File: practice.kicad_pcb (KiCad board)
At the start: 2 copper layers, 100 x 100 mm, 190 parts, among them U1 LTC1742, U10 LTC1742, U2 LTC1742, U3 LTC1742, U4 LTC1742, U5 LTC1742, U6 LTC1742, U7 LTC1742, U8 LTC1742, U9 LTC1742

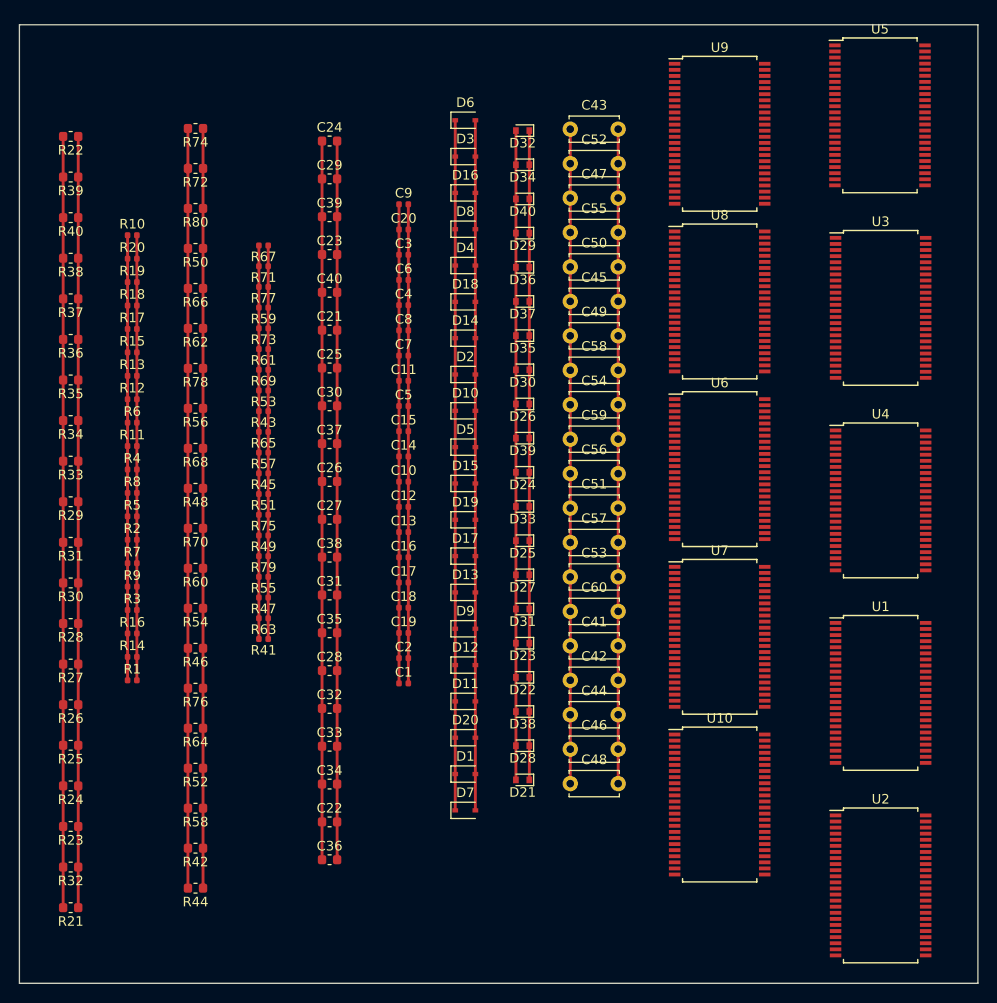
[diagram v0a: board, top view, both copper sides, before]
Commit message: change some part cuz i find them useless
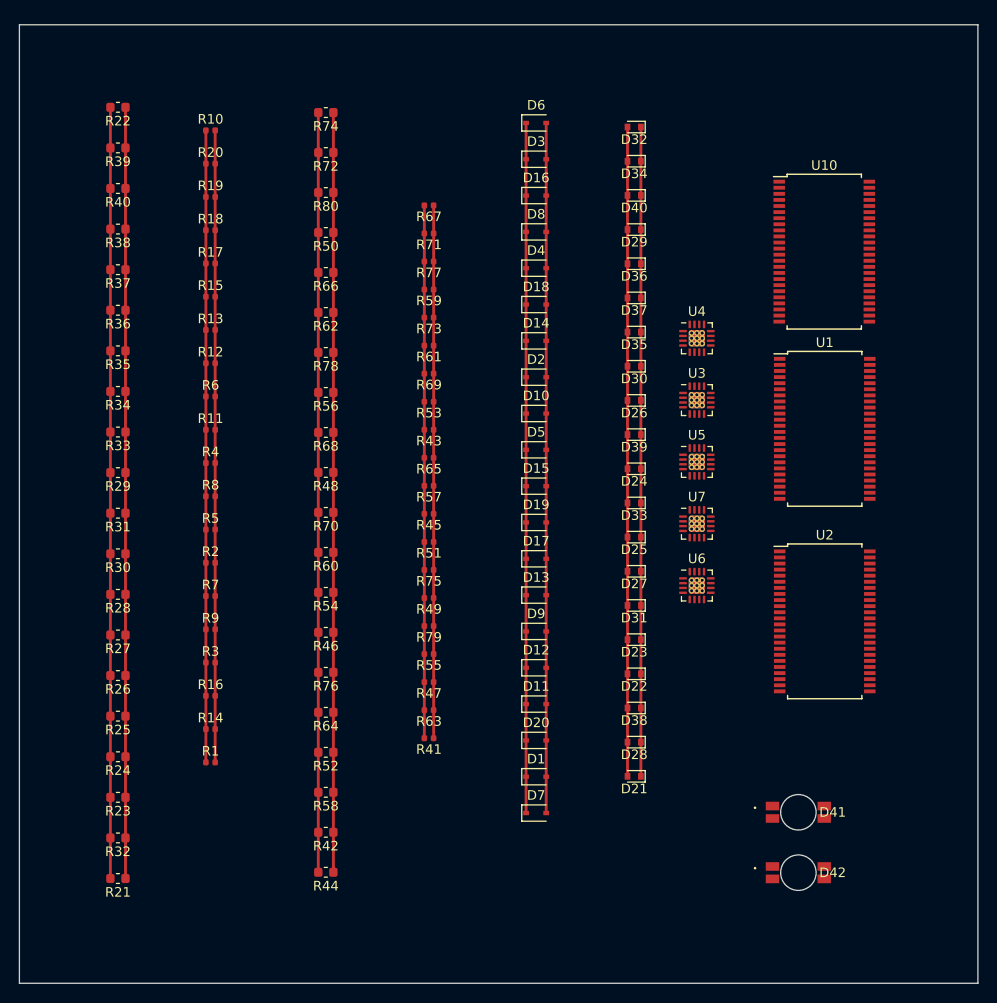
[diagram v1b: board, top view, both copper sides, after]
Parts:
- removed C1, C10, C11, C12, C13, C14, C15, C16, C17, C18, C19, C2, C20, C3, C4, C5, C6, C7, C8, C9: C, Capacitor_SMD:C_0402_1005Metric
- removed C21, C22, C23, C24, C25, C26, C27, C28, C29, C30, C31, C32, C33, C34, C35, C36, C37, C38, C39, C40: C, Capacitor_SMD:C_0603_1608Metric
- removed C41, C42, C43, C44, C45, C46, C47, C48, C49, C50, C51, C52, C53, C54, C55, C56, C57, C58, C59, C60: C, Capacitor_THT:C_Disc_D5.0mm_W2.5mm_P5.00mm
- removed U8, U9: LTC1742, Package_SO:SSOP-48_7.5x15.9mm_P0.635mm
- added D41: LED_RGBA, KiCad:RGB_LED_3528_reverse, F.Cu at (191.2, 115.3)
- added D42: LED_RGBA, KiCad:RGB_LED_3528_reverse, F.Cu at (191.2, 121.6)
- U3, U4, U5, U6, U7: value LTC1742 -> XPT2046QF; footprint Package_SO:SSOP-48_7.5x15.9mm_P0.635mm -> Package_DFN_QFN:QFN-16-1EP_3x3mm_P0.5mm_EP1.7x1.7mm_ThermalVias
- moved U10 58.7 mm to (193.9, 56.8)
- moved U5 40.9 mm to (180.6, 78.8)
- moved U1 28.2 mm to (194.0, 75.3)
- moved U2 28.2 mm to (194.0, 95.4)
- moved U4 25.6 mm to (180.6, 65.9)
- moved U3 21.5 mm to (180.6, 72.3)
- moved R41 20.1 mm to (152.7, 107.6)
- moved R63 19.7 mm to (152.7, 104.7)
- moved R47 19.4 mm to (152.7, 101.7)
- moved R55 19.0 mm to (152.7, 98.8)
- moved R79 18.7 mm to (152.7, 95.9)
- moved R49 18.5 mm to (152.7, 93.0)
- moved R75 18.2 mm to (152.7, 90.0)
- moved R51 18.0 mm to (152.7, 87.1)
- moved R45 17.8 mm to (152.7, 84.2)
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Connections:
- U3 pad 12: Net-(U3-Pad12) -> (no net)
- U3 pad 13: Net-(U3-Pad12) -> (no net)
- U3 pad 16: Net-(U3-Pad12) -> (no net)
- U3 pad 3: Net-(U3-Pad12) -> (no net)
- U3 pad 6: Net-(U3-Pad12) -> (no net)
- U3 pad 7: Net-(U3-Pad17) -> (no net)
- U3 pad 8: Net-(U3-Pad17) -> (no net)
- U3 pad 9: Net-(U3-Pad12) -> (no net)
- U4 pad 12: Net-(U4-Pad12) -> (no net)
- U4 pad 13: Net-(U4-Pad12) -> (no net)
- U4 pad 16: Net-(U4-Pad12) -> (no net)
- U4 pad 3: Net-(U4-Pad12) -> (no net)
- U4 pad 6: Net-(U4-Pad12) -> (no net)
- U4 pad 7: Net-(U4-Pad17) -> (no net)
- U4 pad 8: Net-(U4-Pad17) -> (no net)
- U4 pad 9: Net-(U4-Pad12) -> (no net)
- U5 pad 12: Net-(U5-Pad12) -> (no net)
- U5 pad 13: Net-(U5-Pad12) -> (no net)
- U5 pad 16: Net-(U5-Pad12) -> (no net)
- U5 pad 3: Net-(U5-Pad12) -> (no net)
- U5 pad 6: Net-(U5-Pad12) -> (no net)
- U5 pad 7: Net-(U5-Pad17) -> (no net)
- U5 pad 8: Net-(U5-Pad17) -> (no net)
- U5 pad 9: Net-(U5-Pad12) -> (no net)
- U6 pad 12: Net-(U6-Pad12) -> (no net)
- U6 pad 13: Net-(U6-Pad12) -> (no net)
- U6 pad 16: Net-(U6-Pad12) -> (no net)
- U6 pad 3: Net-(U6-Pad12) -> (no net)
- U6 pad 6: Net-(U6-Pad12) -> (no net)
- U6 pad 7: Net-(U6-Pad17) -> (no net)
- U6 pad 8: Net-(U6-Pad17) -> (no net)
- U6 pad 9: Net-(U6-Pad12) -> (no net)
- U7 pad 12: Net-(U7-Pad12) -> (no net)
- U7 pad 13: Net-(U7-Pad12) -> (no net)
- U7 pad 16: Net-(U7-Pad12) -> (no net)
- U7 pad 3: Net-(U7-Pad12) -> (no net)
- U7 pad 6: Net-(U7-Pad12) -> (no net)
- U7 pad 7: Net-(U7-Pad17) -> (no net)
- U7 pad 8: Net-(U7-Pad17) -> (no net)
- U7 pad 9: Net-(U7-Pad12) -> (no net)
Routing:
- net Net-(C21-Pad2): track 75.0 -> 0.00 mm
- net Net-(C21-Pad1): track 75.0 -> 0.00 mm
- net Net-(C41-Pad2): track 68.3 -> 0.00 mm
- net Net-(C41-Pad1): track 68.3 -> 0.00 mm
- net Net-(C1-Pad2): track 50.0 -> 0.00 mm
- net Net-(C1-Pad1): track 50.0 -> 0.00 mm
- net Net-(R1-Pad2): track 46.4 -> 65.9 mm
- net Net-(R1-Pad1): track 46.4 -> 65.9 mm
- net Net-(R41-Pad2): track 41.0 -> 55.6 mm
- net Net-(R41-Pad1): track 41.0 -> 55.6 mm

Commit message: add some holes for my keyboard(testing)
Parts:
- moved D41 39.0 mm to (152.3, 117.8)
- moved D42 39.0 mm to (152.3, 124.1)
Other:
- outline, holes or cut-outs redrawn
- board text added: "Helloworld"
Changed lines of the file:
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@@
   (general
     (thickness 1.6)
-    (drawings 4)
+    (drawings 32)
     (tracks 18)
     (zones 0)
@@
   )
   (module KiCad:RGB_LED_3528_reverse (layer F.Cu)
-    (at 191.23 121.63)
+    (at 152.28 124.13)
     (descr "LED SMD 1206 (3216 Metric), square (rectangular) end terminal, IPC_7351 nominal, (Body size source: http://www.tortai-tech.com/upload/download/2011102023233369053.pdf), generated with kicad-footprint-generator")
     (tags diode)
@@
   )
   (module KiCad:RGB_LED_3528_reverse (layer F.Cu)
-    (at 191.23 115.33)
+    (at 152.28 117.83)
     (descr "LED SMD 1206 (3216 Metric), square (rectangular) end terminal, IPC_7351 nominal, (Body size source: http://www.tortai-tech.com/upload/download/2011102023233369053.pdf), generated with kicad-footprint-generator")
     (tags diode)
@@
   )
   (module Package_DFN_QFN:QFN-16-1EP_3x3mm_P0.5mm_EP1.7x1.7mm_ThermalVias (layer F.Cu)
-    (at 180.64 85.22625)
+    (at 180.635 85.22625)
     (descr "QFN, 16 Pin (http://www.cypress.com/file/46236/download), generated with kicad-footprint-generator ipc_dfn_qfn_generator.py")
     (tags "QFN DFN_QFN")
@@
   )
   (module Package_DFN_QFN:QFN-16-1EP_3x3mm_P0.5mm_EP1.7x1.7mm_ThermalVias (layer F.Cu)
-    (at 180.64 91.675)
+    (at 180.635 91.675)
     (descr "QFN, 16 Pin (http://www.cypress.com/file/46236/download), generated with kicad-footprint-generator ipc_dfn_qfn_generator.py")
     (tags "QFN DFN_QFN")
@@
   )
   (module Package_DFN_QFN:QFN-16-1EP_3x3mm_P0.5mm_EP1.7x1.7mm_ThermalVias (layer F.Cu)
-    (at 180.64 78.7775)
+    (at 180.635 78.7775)
     (descr "QFN, 16 Pin (http://www.cypress.com/file/46236/download), generated with kicad-footprint-generator ipc_dfn_qfn_generator.py")
     (tags "QFN DFN_QFN")
@@
   )
   (module Package_DFN_QFN:QFN-16-1EP_3x3mm_P0.5mm_EP1.7x1.7mm_ThermalVias (layer F.Cu)
-    (at 180.64 65.88)
+    (at 180.635 65.88)
     (descr "QFN, 16 Pin (http://www.cypress.com/file/46236/download), generated with kicad-footprint-generator ipc_dfn_qfn_generator.py")
     (tags "QFN DFN_QFN")
@@
   )
   (module Package_DFN_QFN:QFN-16-1EP_3x3mm_P0.5mm_EP1.7x1.7mm_ThermalVias (layer F.Cu)
-    (at 180.64 72.32875)
+    (at 180.635 72.32875)
     (descr "QFN, 16 Pin (http://www.cypress.com/file/46236/download), generated with kicad-footprint-generator ipc_dfn_qfn_generator.py")
     (tags "QFN DFN_QFN")
@@
     )
   )
+  (gr_text Helloworld (at 183.46 44.96) (layer B.Cu)
+    (effects (font (size 1.5 1.5) (thickness 0.3)) (justify mirror))
+  )
+  (gr_text Helloworld (at 183.27 42.61) (layer B.Cu)
+    (effects (font (size 1.5 1.5) (thickness 0.3)) (justify mirror))
+  )
+  (gr_text Helloworld (at 182.73 39.41) (layer B.Cu)
+    (effects (font (size 1.5 1.5) (thickness 0.3)) (justify mirror))
+  )
+  (gr_text Helloworld (at 195.73 44.57) (layer B.Cu)
+    (effects (font (size 1.5 1.5) (thickness 0.3)) (justify mirror))
+  )
+  (gr_text Helloworld (at 195.91 42.25) (layer B.Cu)
+    (effects (font (size 1.5 1.5) (thickness 0.3)) (justify mirror))
+  )
+  (gr_text Helloworld (at 196.09 39.41) (layer B.Cu)
+    (effects (font (size 1.5 1.5) (thickness 0.3)) (justify mirror))
+  )
+  (gr_poly (pts (xy 185.45 94.87) (xy 176.66 95.27) (xy 176.8 60.88) (xy 185.43 60.88)) (layer B.Cu) (width 0.1))
+  (gr_poly (pts (xy 181.51 92.56) (xy 179.76 92.57) (xy 179.76 90.81) (xy 181.51 90.81)) (layer B.Mask) (width 0.1))
+  (gr_poly (pts (xy 181.51 86.11) (xy 179.76 86.12) (xy 179.76 84.36) (xy 181.51 84.36)) (layer B.Mask) (width 0.1))
+  (gr_poly (pts (xy 181.51 79.66) (xy 179.76 79.67) (xy 179.76 77.91) (xy 181.51 77.91)) (layer B.Mask) (width 0.1))
+  (gr_poly (pts (xy 181.51 73.21) (xy 179.76 73.22) (xy 179.76 71.46) (xy 181.51 71.46)) (layer B.Mask) (width 0.1))
+  (gr_poly (pts (xy 181.51 66.76) (xy 179.76 66.77) (xy 179.76 65.01) (xy 181.51 65.01)) (layer B.Mask) (width 0.1))
+  (gr_line (start 194 110.38) (end 208 110.38) (layer Edge.Cuts) (width 0.05))
+  (gr_line (start 208 124.38) (end 194 124.38) (layer Edge.Cuts) (width 0.05))
+  (gr_line (start 208 110.38) (end 208 124.38) (layer Edge.Cuts) (width 0.05))
+  (gr_line (start 194 124.38) (end 194 110.38) (layer Edge.Cuts) (width 0.05))
+  (gr_line (start 170.59 122.43) (end 170.59 119.43) (layer Edge.Cuts) (width 0.05))
+  (gr_line (start 167.09 119.43) (end 167.09 122.43) (layer Edge.Cuts) (width 0.05))
+  (gr_line (start 170.59 122.43) (end 167.09 122.43) (layer Edge.Cuts) (width 0.05))
+  (gr_line (start 167.09 119.43) (end 170.59 119.43) (layer Edge.Cuts) (width 0.05))
+  (gr_line (start 166.25 122.44) (end 166.25 119.44) (layer Edge.Cuts) (width 0.05))
+  (gr_line (start 166.25 122.44) (end 162.75 122.44) (layer Edge.Cuts) (width 0.05))
+  (gr_line (start 162.75 119.44) (end 162.75 122.44) (layer Edge.Cuts) (width 0.05))
+  (gr_line (start 162.75 119.44) (end 166.25 119.44) (layer Edge.Cuts) (width 0.05))
+  (gr_line (start 192.33 124.34) (end 178.33 124.34) (layer Edge.Cuts) (width 0.05))
+  (gr_line (start 178.33 124.34) (end 178.33 110.34) (layer Edge.Cuts) (width 0.05))
+  (gr_line (start 192.33 110.34) (end 192.33 124.34) (layer Edge.Cuts) (width 0.05))
+  (gr_line (start 178.33 110.34) (end 192.33 110.34) (layer Edge.Cuts) (width 0.05))
   (gr_line (start 109.96 133.17) (end 109.96 33.17) (layer Edge.Cuts) (width 0.05))
   (gr_line (start 209.96 133.17) (end 109.96 133.17) (layer Edge.Cuts) (width 0.05))
